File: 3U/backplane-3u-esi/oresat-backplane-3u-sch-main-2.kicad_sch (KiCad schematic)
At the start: 16 parts

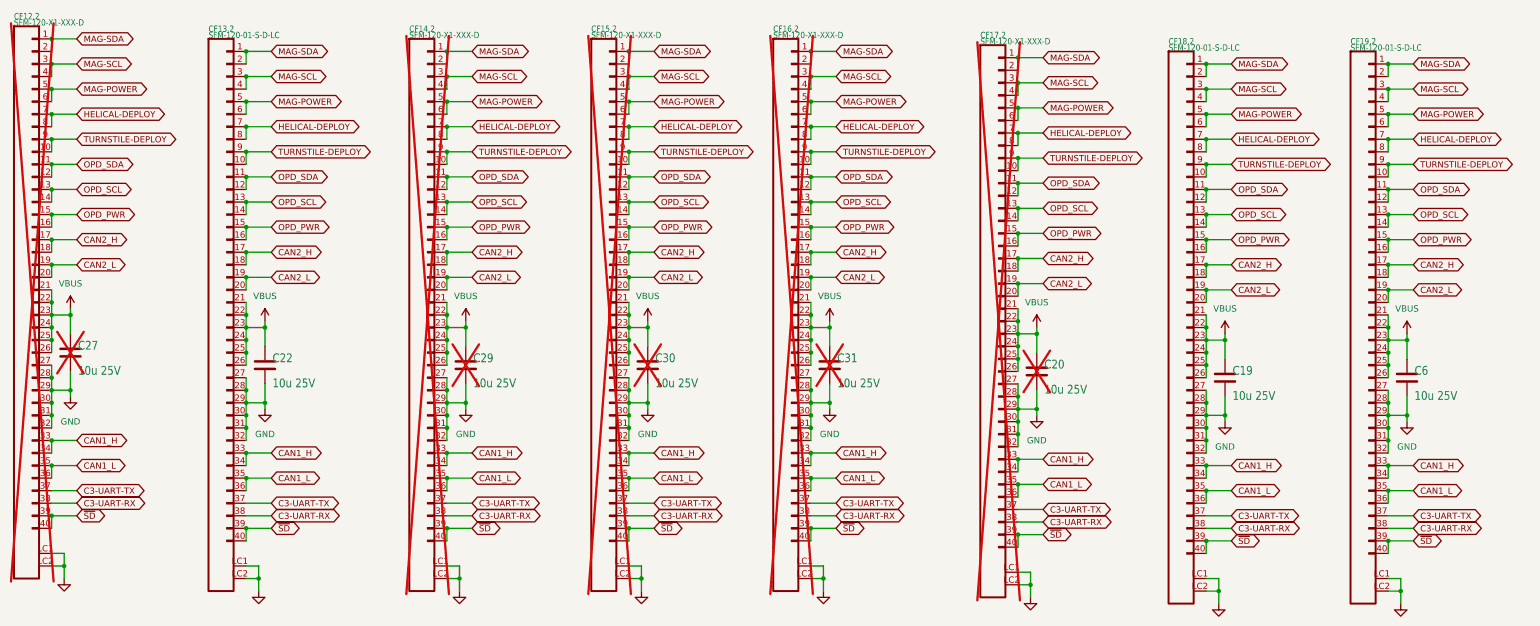
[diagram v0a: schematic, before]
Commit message: Changed schematic & pcb to add spare traces, no helical or turnstile
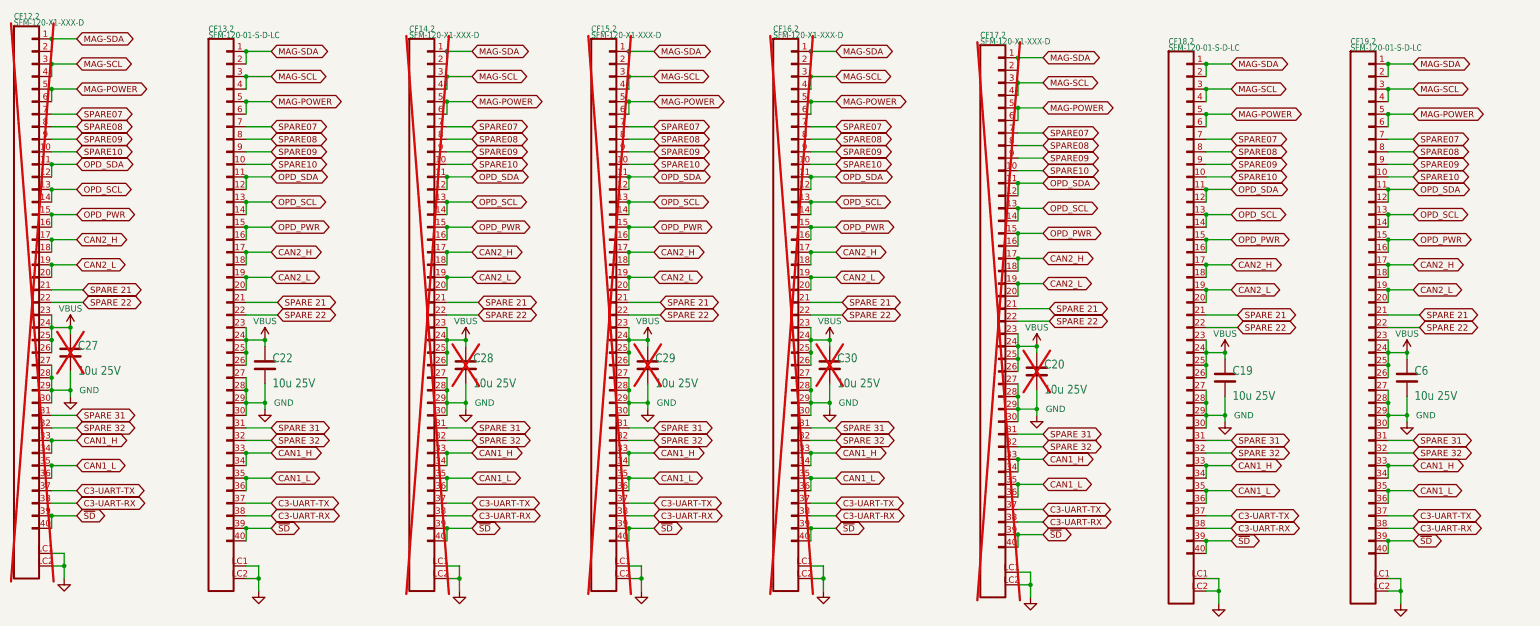
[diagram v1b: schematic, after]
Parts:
- removed C31: 10u 25V, Capacitor_SMD:C_1206_3216Metric, symbol Device:C
- added C28: 10u 25V, Capacitor_SMD:C_1206_3216Metric, symbol Device:C
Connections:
- net GND: now also C28.2; no longer CF12.2.31, CF12.2.32, CF13.2.31, CF13.2.32, CF14.2.31, CF14.2.32, CF15.2.31, CF15.2.32, CF16.2.31, CF16.2.32, CF17.2.31, CF17.2.32, CF18.2.31, CF18.2.32, CF19.2.31, CF19.2.32
- net VBUS: now also C28.1; no longer CF12.2.21, CF12.2.22, CF13.2.21, CF13.2.22, CF14.2.21, CF14.2.22, CF15.2.21, CF15.2.22, CF16.2.21, CF16.2.22, CF17.2.21, CF17.2.22, CF18.2.21, CF18.2.22, CF19.2.21, CF19.2.22
- net HELICAL-DEPLOY renamed SPARE07
- net SPARE07: no longer CF12.2.8, CF13.2.8, CF14.2.8, CF15.2.8, CF16.2.8, CF17.2.8, CF18.2.8, CF19.2.8
- net TURNSTILE-DEPLOY renamed SPARE09
- net SPARE09: no longer CF12.2.10, CF13.2.10, CF14.2.10, CF15.2.10, CF16.2.10, CF17.2.10, CF18.2.10, CF19.2.10
- new net SPARE 21: CF12.2.21, CF13.2.21, CF14.2.21, CF15.2.21, CF16.2.21, CF17.2.21, CF18.2.21, CF19.2.21
- new net SPARE 22: CF12.2.22, CF13.2.22, CF14.2.22, CF15.2.22, CF16.2.22, CF17.2.22, CF18.2.22, CF19.2.22
- new net SPARE 31: CF12.2.31, CF13.2.31, CF14.2.31, CF15.2.31, CF16.2.31, CF17.2.31, CF18.2.31, CF19.2.31
- new net SPARE 32: CF12.2.32, CF13.2.32, CF14.2.32, CF15.2.32, CF16.2.32, CF17.2.32, CF18.2.32, CF19.2.32
- new net SPARE08: CF12.2.8, CF13.2.8, CF14.2.8, CF15.2.8, CF16.2.8, CF17.2.8, CF18.2.8, CF19.2.8
- new net SPARE10: CF12.2.10, CF13.2.10, CF14.2.10, CF15.2.10, CF16.2.10, CF17.2.10, CF18.2.10, CF19.2.10
